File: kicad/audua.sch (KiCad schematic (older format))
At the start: 2 parts

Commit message: Most things
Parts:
- added BT?: BATTERY, ~, symbol BATTERY
- added D?: LED, ~, symbol LED
- added MIC?: SPU0414HR5H-SB, ~, symbol SPU0414HR5H-SB
- added SW?: SWITCH_INV, ~, symbol SWITCH_INV
- added U?: MICROSD, ~, symbol MICROSD
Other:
- moved on the sheet: U?
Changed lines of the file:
@@
 LIBS:valves
 LIBS:stm32l051xx
-EELAYER 24 0
+LIBS:spu0414hr5h-sb
+LIBS:microsd
+LIBS:audua-cache
+EELAYER 27 0
 EELAYER END
 $Descr A4 11693 8268
@@
 Sheet 1 1
 Title ""
-Date ""
+Date "14 jun 2014"
 Rev ""
 Comp ""
@@
 L STM32L051-32QFN U?
 U 1 1 53988104
-P 4400 2850
-F 0 "U?" H 4400 2700 50  0000 C CNN
-F 1 "STM32L051-32QFN" H 4400 2850 50  0000 C CNN
-F 2 "MODULE" H 4400 2850 50  0001 C CNN
-F 3 "DOCUMENTATION" H 4400 2850 50  0001 C CNN
-	1    4400 2850
+P 8200 3900
+F 0 "U?" H 8200 3750 50  0000 C CNN
+F 1 "STM32L051-32QFN" H 8200 3900 50  0000 C CNN
+F 2 "MODULE" H 8200 3900 50  0001 C CNN
+F 3 "DOCUMENTATION" H 8200 3900 50  0001 C CNN
+	1    8200 3900
 	1    0    0    -1
 $EndComp
@@
 L GND #PWR?
 U 1 1 53988118
-P 4950 3850
-F 0 "#PWR?" H 4950 3850 30  0001 C CNN
-F 1 "GND" H 4950 3780 30  0001 C CNN
-F 2 "" H 4950 3850 60  0000 C CNN
-F 3 "" H 4950 3850 60  0000 C CNN
-	1    4950 3850
-	1    0    0    -1
-$EndComp
-Wire Wire Line
-	4950 3850 4950 3800
+P 8750 4900
+F 0 "#PWR?" H 8750 4900 30  0001 C CNN
+F 1 "GND" H 8750 4830 30  0001 C CNN
+F 2 "" H 8750 4900 60  0000 C CNN
+F 3 "" H 8750 4900 60  0000 C CNN
+	1    8750 4900
+	1    0    0    -1
+$EndComp
+Wire Wire Line
+	8750 4900 8750 4850
 $Comp
 L VDD #PWR?
 U 1 1 5398812E
-P 3350 2400
-F 0 "#PWR?" H 3350 2500 30  0001 C CNN
-F 1 "VDD" H 3350 2510 30  0000 C CNN
-F 2 "" H 3350 2400 60  0000 C CNN
-F 3 "" H 3350 2400 60  0000 C CNN
-	1    3350 2400
-	1    0    0    -1
-$EndComp
-Wire Wire Line
-	3350 2400 3350 2500
-Wire Wire Line
-	3350 2500 3450 2500
+P 7150 3450
+F 0 "#PWR?" H 7150 3550 30  0001 C CNN
+F 1 "VDD" H 7150 3560 30  0000 C CNN
+F 2 "" H 7150 3450 60  0000 C CNN
+F 3 "" H 7150 3450 60  0000 C CNN
+	1    7150 3450
+	1    0    0    -1
+$EndComp
+Wire Wire Line
+	7150 3450 7150 3550
+Wire Wire Line
+	7150 3550 7250 3550
 $Comp
 L VDD #PWR?
 U 1 1 53988145
-P 5550 3150
-F 0 "#PWR?" H 5550 3250 30  0001 C CNN
-F 1 "VDD" H 5550 3260 30  0000 C CNN
-F 2 "" H 5550 3150 60  0000 C CNN
-F 3 "" H 5550 3150 60  0000 C CNN
-	1    5550 3150
-	1    0    0    -1
-$EndComp
-Wire Wire Line
-	5550 3150 5550 3200
-Wire Wire Line
-	5550 3200 5350 3200
+P 9350 4200
+F 0 "#PWR?" H 9350 4300 30  0001 C CNN
+F 1 "VDD" H 9350 4310 30  0000 C CNN
+F 2 "" H 9350 4200 60  0000 C CNN
+F 3 "" H 9350 4200 60  0000 C CNN
+	1    9350 4200
+	1    0    0    -1
+$EndComp
+Wire Wire Line
+	9350 4200 9350 4250
+Wire Wire Line
+	9350 4250 9150 4250
 $Comp
 L GND #PWR?
 U 1 1 53988167
-P 4200 1850
-F 0 "#PWR?" H 4200 1850 30  0001 C CNN
-F 1 "GND" H 4200 1780 30  0001 C CNN
-F 2 "" H 4200 1850 60  0000 C CNN
-F 3 "" H 4200 1850 60  0000 C CNN
-	1    4200 1850
-	1    0    0    -1
-$EndComp
-Wire Wire Line
-	4200 1850 4200 1750
-Wire Wire Line
-	4200 1750 4150 1750
-Wire Wire Line
-	4150 1750 4150 1900
-NoConn ~ 3450 2800
+P 8000 2900
+F 0 "#PWR?" H 8000 2900 30  0001 C CNN
+F 1 "GND" H 8000 2830 30  0001 C CNN
+F 2 "" H 8000 2900 60  0000 C CNN
+F 3 "" H 8000 2900 60  0000 C CNN
+	1    8000 2900
+	1    0    0    -1
+$EndComp
+Wire Wire Line
+	8000 2900 8000 2800
+Wire Wire Line
+	8000 2800 7950 2800
+Wire Wire Line
+	7950 2800 7950 2950
+NoConn ~ 7250 3850
 $Comp
 L VDD #PWR?
 U 1 1 53988198
-P 3350 2850
-F 0 "#PWR?" H 3350 2950 30  0001 C CNN
-F 1 "VDD" H 3350 2960 30  0000 C CNN
-F 2 "" H 3350 2850 60  0000 C CNN
-F 3 "" H 3350 2850 60  0000 C CNN
-	1    3350 2850
-	1    0    0    -1
-$EndComp
-Wire Wire Line
-	3350 2850 3350 2900
-Wire Wire Line
-	3350 2900 3450 2900
-NoConn ~ 3450 2600
-NoConn ~ 3450 2700
-Wire Wire Line
-	5350 2500 5900 2500
-Text Label 5900 2500 2    60   ~ 0
+P 7150 3900
+F 0 "#PWR?" H 7150 4000 30  0001 C CNN
+F 1 "VDD" H 7150 4010 30  0000 C CNN
+F 2 "" H 7150 3900 60  0000 C CNN
+F 3 "" H 7150 3900 60  0000 C CNN
+	1    7150 3900
+	1    0    0    -1
+$EndComp
+Wire Wire Line
+	7150 3900 7150 3950
+Wire Wire Line
+	7150 3950 7250 3950
+NoConn ~ 7250 3650
+NoConn ~ 7250 3750
+Wire Wire Line
+	9150 3550 9700 3550
+Text Label 9700 3550 2    60   ~ 0
 SWCLK
 Wire Wire Line
-	5350 2600 5900 2600
-Text Label 5900 2600 2    60   ~ 0
+	9150 3650 9700 3650
+Text Label 9700 3650 2    60   ~ 0
 SWDIO
 $Comp
@@
 Text Label 6400 1400 0    60   ~ 0
 SWDAT
+$Comp
+L SPU0414HR5H-SB MIC?
+U 1 1 539CB6C0
+P 1700 1850
+F 0 "MIC?" H 1700 1800 60  0000 C CNN
+F 1 "SPU0414HR5H-SB" H 1700 1900 60  0000 C CNN
+F 2 "~" H 1700 1850 60  0000 C CNN
+F 3 "~" H 1700 1850 60  0000 C CNN
+	1    1700 1850
+	1    0    0    -1
+$EndComp
+$Comp
+L BATTERY BT?
+U 1 1 539CB7D1
+P 5450 2700
+F 0 "BT?" H 5450 2900 50  0000 C CNN
+F 1 "BATTERY" H 5450 2510 50  0000 C CNN
+F 2 "~" H 5450 2700 60  0000 C CNN
+F 3 "~" H 5450 2700 60  0000 C CNN
+	1    5450 2700
+	1    0    0    -1
+$EndComp
+$Comp
+L MICROSD U?
+U 1 1 539CBD26
+P 3200 4350
+F 0 "U?" V 3300 4350 60  0000 C CNN
+F 1 "MICROSD" V 3200 4350 60  0000 C CNN
+F 2 "~" H 3200 4300 60  0000 C CNN
+F 3 "~" H 3200 4300 60  0000 C CNN
+	1    3200 4350
+	1    0    0    -1
+$EndComp
+$Comp
+L SWITCH_INV SW?
+U 1 1 539CBD3F
+P 5300 4250
+F 0 "SW?" H 5100 4400 50  0000 C CNN
+F 1 "SWITCH_INV" H 5150 4100 50  0000 C CNN
+F 2 "~" H 5300 4250 60  0000 C CNN
+F 3 "~" H 5300 4250 60  0000 C CNN
+	1    5300 4250
+	1    0    0    -1
+$EndComp
+$Comp
+L LED D?
+U 1 1 539CBD58
+P 5050 5050
+F 0 "D?" H 5050 5150 50  0000 C CNN
+F 1 "LED" H 5050 4950 50  0000 C CNN
+F 2 "~" H 5050 5050 60  0000 C CNN
+F 3 "~" H 5050 5050 60  0000 C CNN
+	1    5050 5050
+	1    0    0    -1
+$EndComp
 $EndSCHEMATC

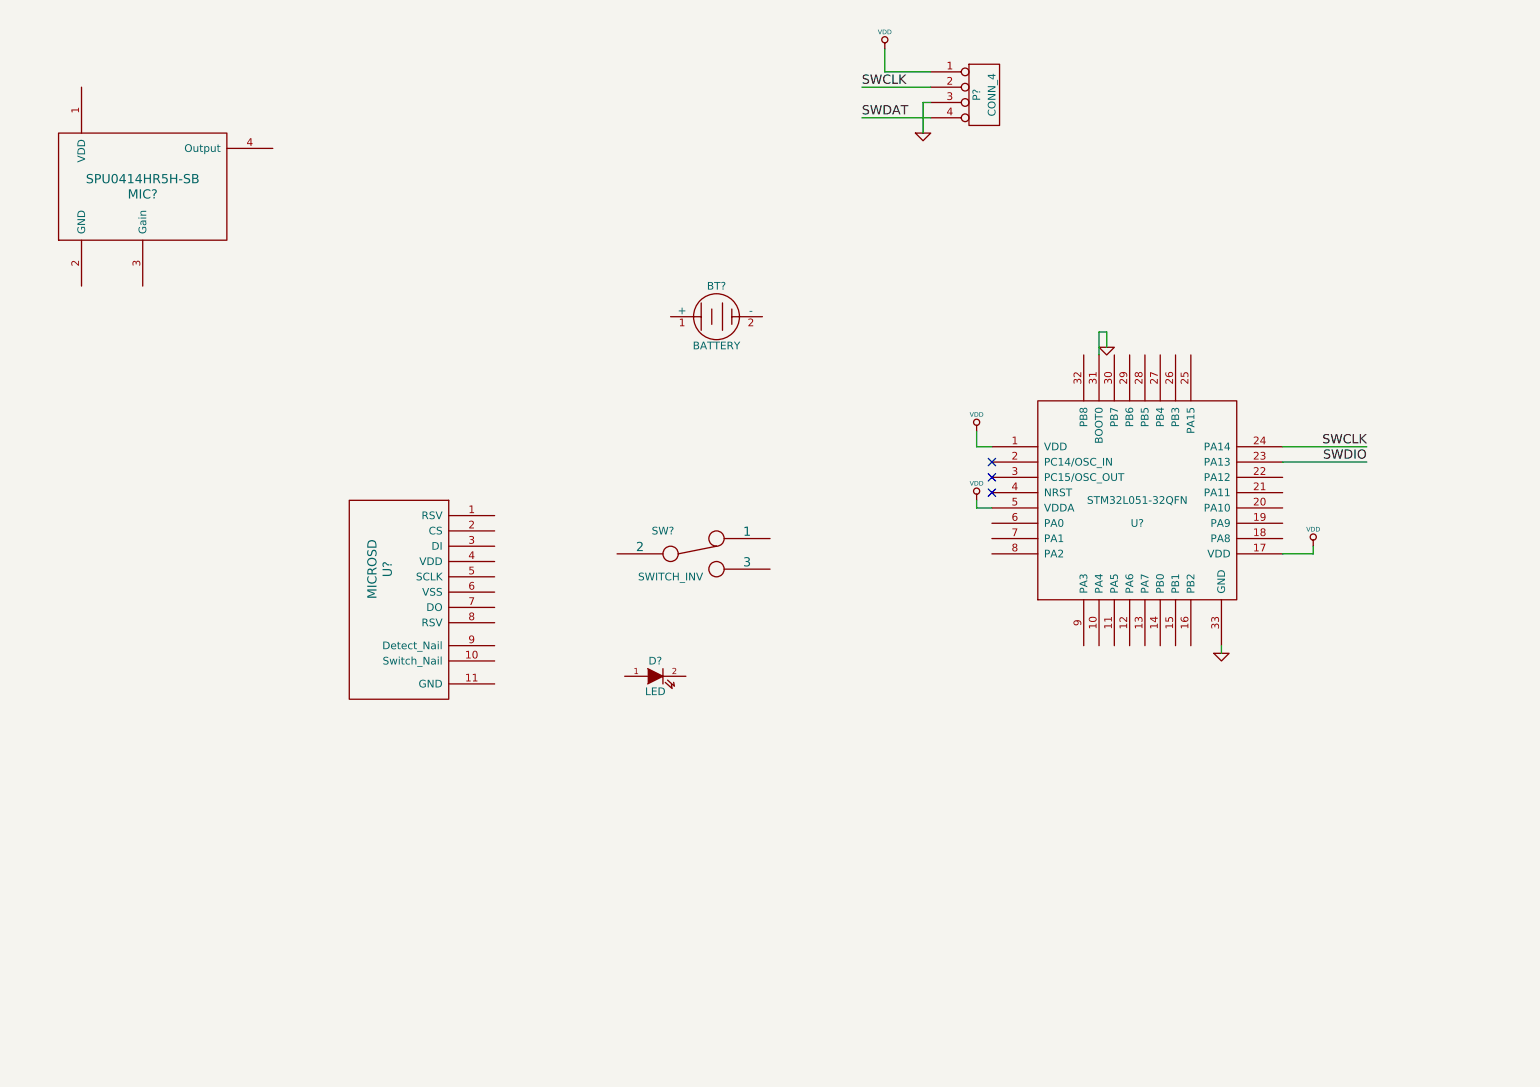
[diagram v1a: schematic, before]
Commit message: Added buck converter
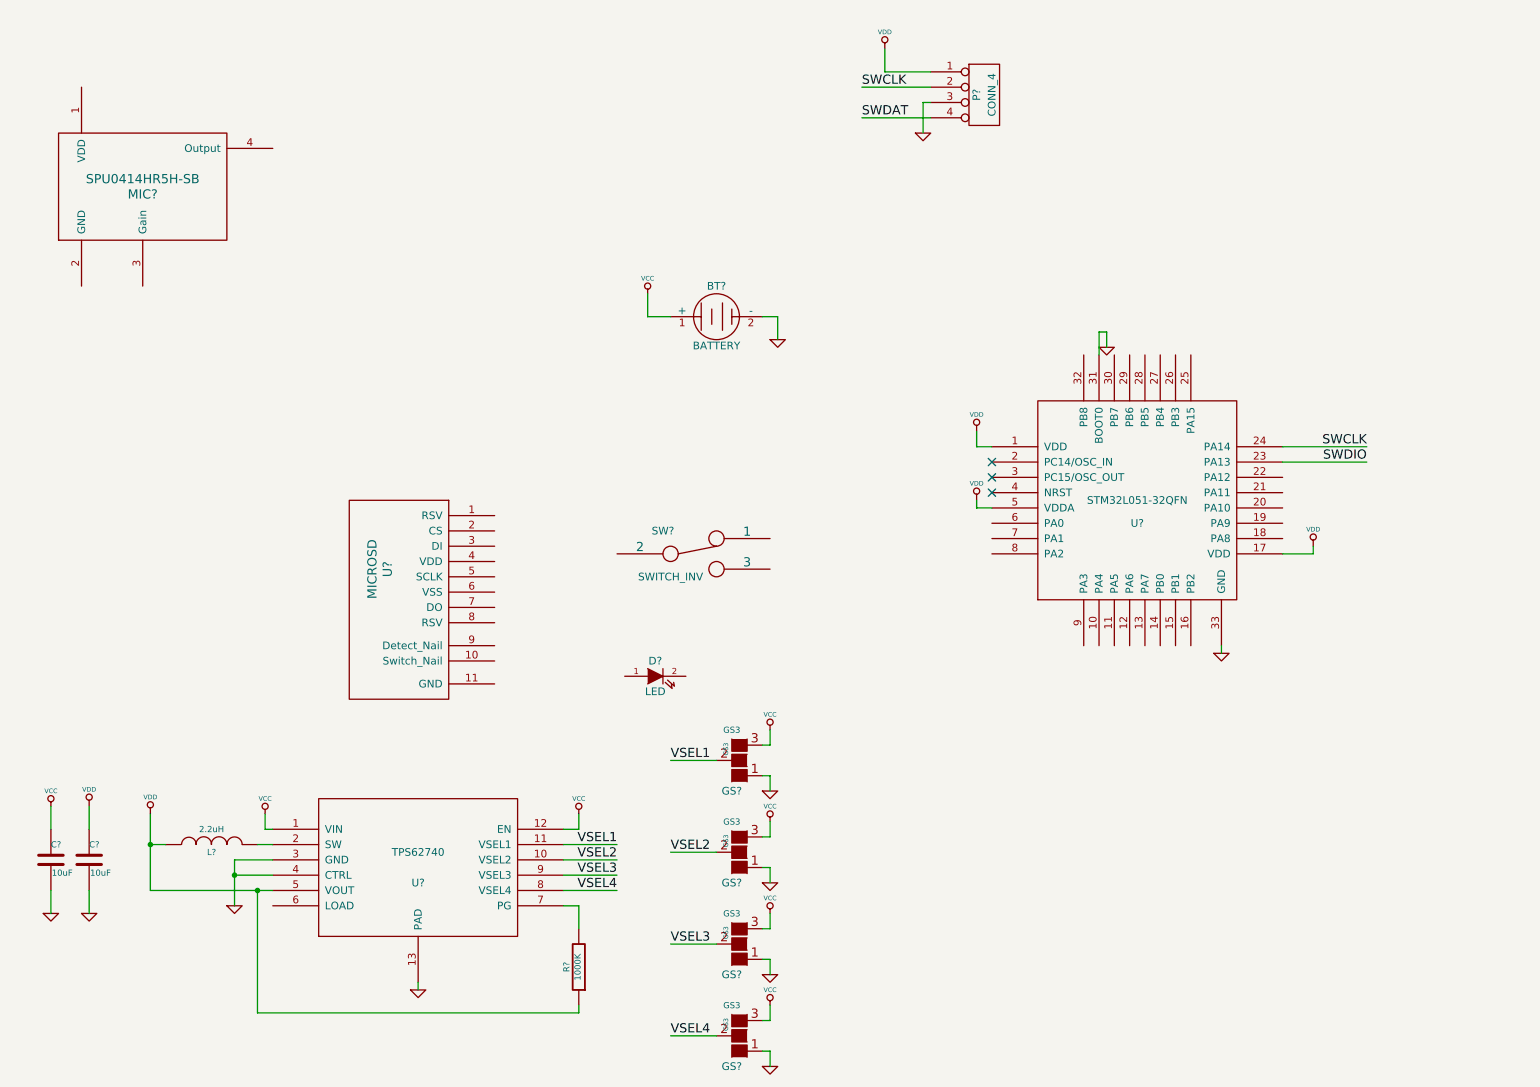
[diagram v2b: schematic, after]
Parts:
- added C? (x2): 10uF, symbol C
- added GS? (x4): GS3, GS3, symbol GS3
- added L?: 2.2uH, symbol INDUCTOR
- added R?: 1000K, symbol R
- added U?: TPS62740, MODULE, symbol TPS62740
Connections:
- net GND: now also BT?.2 (-), C?.2, C?.2, GS?.1 (G1), GS?.1 (G1), GS?.1 (G1), GS?.1 (G1), U?.13 (PAD), U?.3 (GND), U?.4 (CTRL)
- net VDD: now also C?.1, L?.1, R?.1, U?.5 (VOUT)
- net VCC: now reaches BT?.1 (+)
- net VCC: now also C?.1, GS?.3 (G3), GS?.3 (G3), GS?.3 (G3), GS?.3 (G3), U?.1 (VIN), U?.12 (EN)
- new net: L?.2, U?.2 (SW)
- new net: R?.2, U?.7 (PG)
- new net VSEL1: GS?.2 (G2), U?.11 (VSEL1)
- new net VSEL2: GS?.2 (G2), U?.10 (VSEL2)
- new net VSEL3: GS?.2 (G2), U?.9 (VSEL3)
- new net VSEL4: GS?.2 (G2), U?.8 (VSEL4)

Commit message: Not Sure.
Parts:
- removed SW?: SWITCH_INV, ~, symbol SWITCH_INV
- added C1, C2, C3, C4, C5, C6, C7: C, ~, symbol C
- added C8: 50uF, ~, symbol C
- added P2, P3, P4, P5, P6: CONN_1, symbol CONN_1
- added R1, R2: R, ~, symbol R
- added SW1: SPST, ~, symbol SPST
- gave numbers to parts that had none: 15
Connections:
- net SWDAT is gone; now on net SWDIO: P1.4 (P4)
- net GND: now also D1.2 (K), MIC1.2 (GND), U2.11 (GND), U2.6 (VSS), C1.2, C3.2, C4.2, C5.2, C6.2, C7.2, C8.2
- net VDD: now also MIC1.1 (VDD), U2.4 (VDD), U2.9 (Detect_Nail), C1.1, C3.1, C4.1, C5.1, C6.1, C7.1, SW1.1
- net SPI1_NSS: now reaches U1.10 (PA4)
- net SPI1_NSS: now also U2.2 (CS)
- net SPI1_SCK: now reaches U1.11 (PA5)
- net SPI1_SCK: now also U2.5 (SCLK)
- net SPI1_MISO: now reaches U1.12 (PA6)
- net SPI1_MISO: now also U2.7 (DO)
- net SPI1_MOSI: now reaches U1.13 (PA7)
- net SPI1_MOSI: now also U2.3 (DI)
- net at U1.15 (PB1): now also P4.1
- net at U1.16 (PB2): now also P5.1
- net at U1.21 (PA11): now also P3.1
- net at U1.22 (PA12): now also P2.1
- net MIC_OUT: now reaches U1.6 (PA0)
- net MIC_OUT: now also C2.2, P6.1
- net at U1.7 (PA1): now also SW1.2
- net at U1.8 (PA2): now also R2.2
- net at MIC1.3 (Gain): now also R1.1
- net at MIC1.4 (Output): now also C2.1
- net SD_Detect: now reaches U2.10 (Switch_Nail)
- net at D1.1 (A): now also R2.1
- new net: C8.1, R1.2
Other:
- moved on the sheet: BT1, C10, C9, D1, GS1, GS2, GS3, GS4, L1, MIC1, P1, R3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

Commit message: Done?!
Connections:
- net SD_Detect: now also P4.1, U1.15 (PB1)
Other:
- moved on the sheet: P4
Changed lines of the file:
@@
 Sheet 1 1
 Title ""
-Date "15 jun 2014"
+Date "2 jul 2014"
 Rev ""
 Comp ""
@@
 L CONN_1 P4
 U 1 1 539CF245
-P 6950 4550
-F 0 "P4" H 7030 4550 40  0000 L CNN
-F 1 "CONN_1" H 6950 4605 30  0001 C CNN
-F 2 "" H 6950 4550 60  0000 C CNN
-F 3 "" H 6950 4550 60  0000 C CNN
-	1    6950 4550
+P 6950 5000
+F 0 "P4" H 7030 5000 40  0000 L CNN
+F 1 "CONN_1" H 6950 5055 30  0001 C CNN
+F 2 "" H 6950 5000 60  0000 C CNN
+F 3 "" H 6950 5000 60  0000 C CNN
+	1    6950 5000
 	0    1    1    0
 $EndComp
@@
 $EndComp
 Wire Wire Line
-	6950 4300 6950 4400
+	6950 4300 6950 4850
 Wire Wire Line
 	7050 4300 7050 4400
@@
 Wire Wire Line
 	10050 6850 10050 6900
+Text Label 7100 4850 0    60   ~ 0
+SD_Detect
+Wire Wire Line
+	6950 4850 7100 4850
 $EndSCHEMATC
